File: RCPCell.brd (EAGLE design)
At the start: 99.8 x 44.5 mm, 28 parts, among them IC1 SIM900, U1 PESDXS4UD, U7 FAN8303

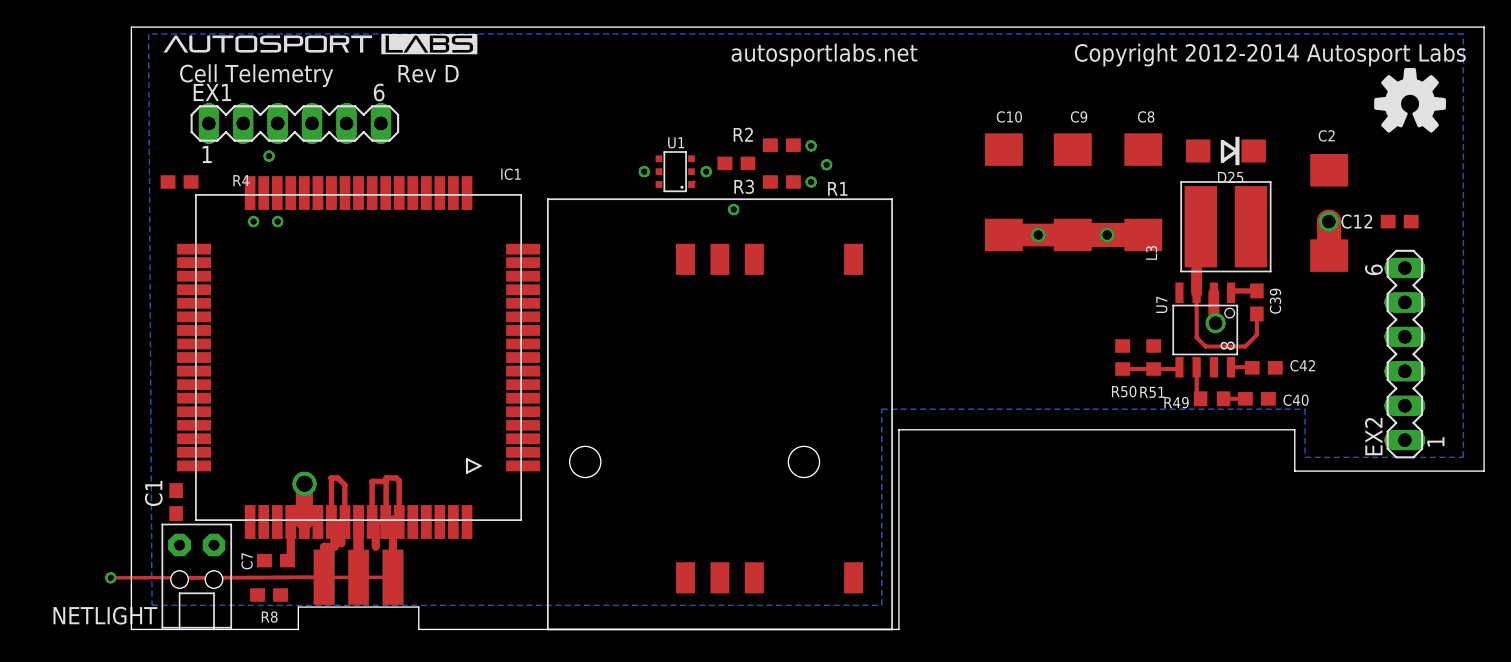
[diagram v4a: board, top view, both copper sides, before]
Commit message: flipped components on cell module to top side
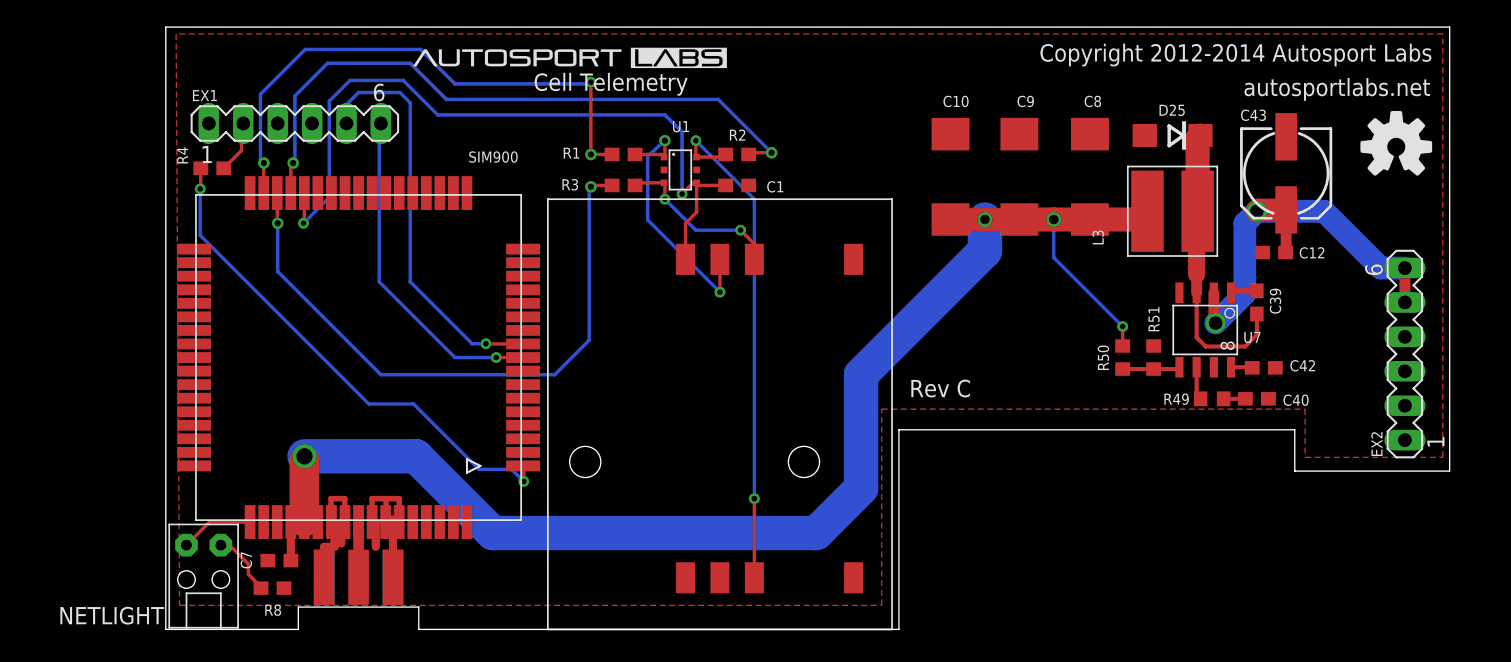
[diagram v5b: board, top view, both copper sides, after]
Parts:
- removed C2: 47uF, rcl:SMC_D
- added C43: 22uF, rcl:153CLV-0605
- moved C1 47.5 mm to (44.7, 32.8), turned to 0 degrees
- moved R1 11.9 mm to (36.3, 35.1), turned to 0 degrees
- moved C12 9.55 mm to (84.3, 27.8)
- moved R3 8.49 mm to (36.3, 32.8), turned to 0 degrees
- moved D25 4.10 mm to (76.8, 36.4)
- moved L3 4.10 mm to (76.8, 30.9)
- moved C10 4.10 mm to (60.5, 33.4)
- moved C8 4.10 mm to (70.7, 33.4)
- moved C9 4.10 mm to (65.5, 33.4)
- moved R2 3.37 mm to (44.7, 35.1)
- moved R4 2.62 mm to (5.97, 34.0), turned to 0 degrees
- moved R8 0.57 mm to (10.4, 3.05)
- moved NETLIGHT 0.51 mm to (5.33, 4.57)
- moved U1 0.40 mm to (40.5, 33.9), turned to 270 degrees
- moved C7 0.25 mm to (10.9, 5.08)
- renumbered IC1 to SIM900
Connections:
- removed net N$2: C1.2, EX1.1, EX2.1, EX2.2, J$1.GND@0, J$1.GND@1, J$1.GND@2, J$1.GND@3, R8.1, SIM900.17, SIM900.18, SIM900.29, SIM900.39, SIM900.45, SIM900.46, SIM900.53, SIM900.54, SIM900.58, SIM900.59, SIM900.61, SIM900.62, SIM900.63, SIM900.64, SIM900.65, U$1.3, U1.2, U1.5
- net GND: now also C1.2, C43.-, EX1.1, EX2.1, EX2.2, J$1.GND@0, J$1.GND@1, J$1.GND@2, J$1.GND@3, R8.1, SIM900.17, SIM900.18, SIM900.29, SIM900.39, SIM900.45, SIM900.46, SIM900.53, SIM900.54, SIM900.58, SIM900.59, SIM900.61, SIM900.62, SIM900.63, SIM900.64, SIM900.65, U$1.6, U1.2, U1.5; no longer C2.-
- net SAFE12V: now also C43.+; no longer C2.+
- net SIM_CLK_CARD: now also U$1.3; no longer U$1.6
- net SIM_DATA_CARD: now also U$1.4; no longer U$1.1
- net SIM_RST_CARD: now also U$1.2; no longer U$1.5
- net SIM_VDD: now also U$1.1; no longer U$1.4
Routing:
- net V+: track 20.3 -> 104.3 mm, vias 3 -> 4
- net N$2: track 60.5 -> 0.00 mm, vias 4 -> 0
- net SIM_VDD: track 0.00 -> 54.5 mm, vias 0 -> 2
- net SIM_DATA: track 0.00 -> 47.9 mm
- net SIM_CLK: track 0.00 -> 46.1 mm
- net SIM_RST: track 0.00 -> 41.2 mm, vias 2 -> 3
- net PWRKEY: track 0.00 -> 37.5 mm, vias 0 -> 2
- net SIM_DATA_CARD: track 0.00 -> 37.5 mm, vias 0 -> 2
- net DIN: track 0.00 -> 30.2 mm, vias 0 -> 1
- net SAFE12V: track 4.81 -> 32.3 mm
- net DOUT: track 0.00 -> 24.7 mm, vias 0 -> 1
- net GND: track 0.00 -> 22.0 mm
- net SIM_RST_CARD: track 0.27 -> 19.8 mm, vias 1 -> 2
- net SIM_CLK_CARD: track 0.00 -> 12.6 mm, vias 0 -> 2
- net N$1000: track 11.6 -> 21.6 mm
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- added copper zone on layer 1, net GND
- removed copper zone on layer 16, net N$2
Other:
- board size 99.8 x 44.5 mm -> 94.7 x 44.5 mm
- board text added: "Rev C"
- board text removed: "Rev D"
